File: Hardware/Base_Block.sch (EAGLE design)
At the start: 46 parts, among them Q1 BSS138, U2 FTS31XS-U, U4 TPS62065

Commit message: file cleanup
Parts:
- L1: value (none) -> 1.0uH
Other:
- moved on the sheet: C8
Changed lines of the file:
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@@
 <part name="C9" library="SparkFun-Capacitors" deviceset="4.7UF-6.3V-10%(0603)" device="0603" value="4.7uF"/>
 <part name="GND10" library="SparkFun-Aesthetics" deviceset="GND" device=""/>
-<part name="L1" library="SparkFun-Passives" deviceset="INDUCTOR" device=""/>
+<part name="L1" library="SparkFun-Passives" deviceset="INDUCTOR" device="" value="1.0uH"/>
 <part name="FID1" library="SparkFun-Aesthetics" deviceset="FIDUCIAL" device="1X2"/>
 <part name="FID2" library="SparkFun-Aesthetics" deviceset="FIDUCIAL" device="1X2"/>
@@
 <instance part="D4" gate="G$1" x="27.94" y="78.74" rot="R90"/>
 <instance part="SUPPLY3" gate="G$1" x="27.94" y="86.36"/>
-<instance part="C8" gate="G$1" x="38.1" y="66.04"/>
-<instance part="GND17" gate="1" x="38.1" y="50.8"/>
+<instance part="C8" gate="G$1" x="40.64" y="66.04"/>
+<instance part="GND17" gate="1" x="40.64" y="50.8"/>
 <instance part="U$1" gate="G$1" x="81.28" y="68.58" rot="MR0"/>
 <instance part="GND18" gate="1" x="60.96" y="50.8"/>
@@
 <pinref part="C8" gate="G$1" pin="2"/>
 <pinref part="GND17" gate="1" pin="GND"/>
-<wire x1="38.1" y1="53.34" x2="38.1" y2="63.5" width="0.1524" layer="91"/>
+<wire x1="40.64" y1="53.34" x2="40.64" y2="63.5" width="0.1524" layer="91"/>
 </segment>
 <segment>
@@
 <pinref part="L1" gate="G$1" pin="2"/>
 <wire x1="200.66" y1="83.82" x2="200.66" y2="86.36" width="0.1524" layer="91"/>
+<junction x="218.44" y="86.36"/>
 </segment>
 <segment>
@@
 <wire x1="27.94" y1="73.66" x2="27.94" y2="76.2" width="0.1524" layer="91"/>
 <pinref part="D4" gate="G$1" pin="A"/>
-<wire x1="27.94" y1="73.66" x2="38.1" y2="73.66" width="0.1524" layer="91"/>
+<wire x1="27.94" y1="73.66" x2="40.64" y2="73.66" width="0.1524" layer="91"/>
 <junction x="27.94" y="73.66"/>
 <pinref part="C8" gate="G$1" pin="1"/>
-<wire x1="38.1" y1="71.12" x2="38.1" y2="73.66" width="0.1524" layer="91"/>
+<wire x1="40.64" y1="71.12" x2="40.64" y2="73.66" width="0.1524" layer="91"/>
 <pinref part="U$1" gate="G$1" pin="VOUT"/>
-<wire x1="38.1" y1="73.66" x2="63.5" y2="73.66" width="0.1524" layer="91"/>
-<junction x="38.1" y="73.66"/>
+<wire x1="40.64" y1="73.66" x2="63.5" y2="73.66" width="0.1524" layer="91"/>
+<junction x="40.64" y="73.66"/>
 <label x="45.72" y="73.66" size="1.778" layer="95"/>
 </segment>

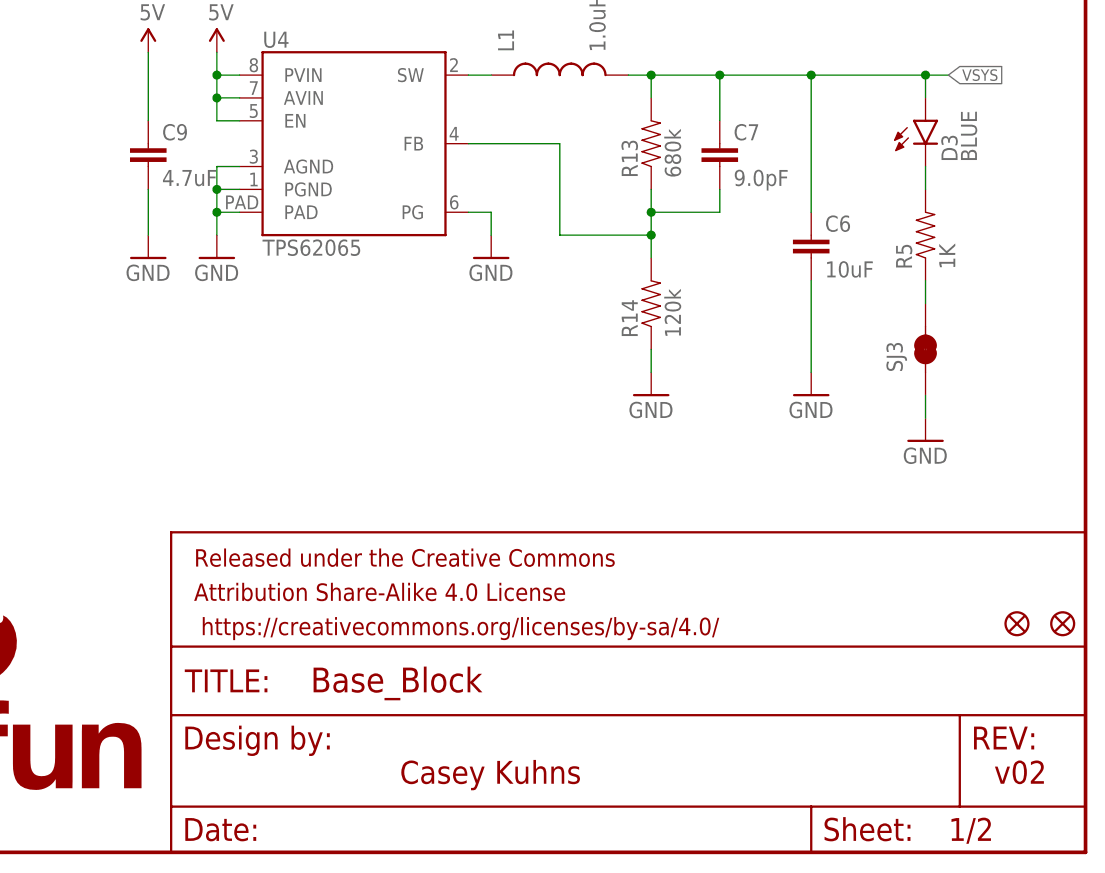
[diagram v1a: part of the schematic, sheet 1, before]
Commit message: Modified Footprint for connectors, removed jumpers. changed version number corrected silk moved diode to help AOI removed jumpers from power supply replaced input and output capacitors on power supply. replaced filtercap with 47pf
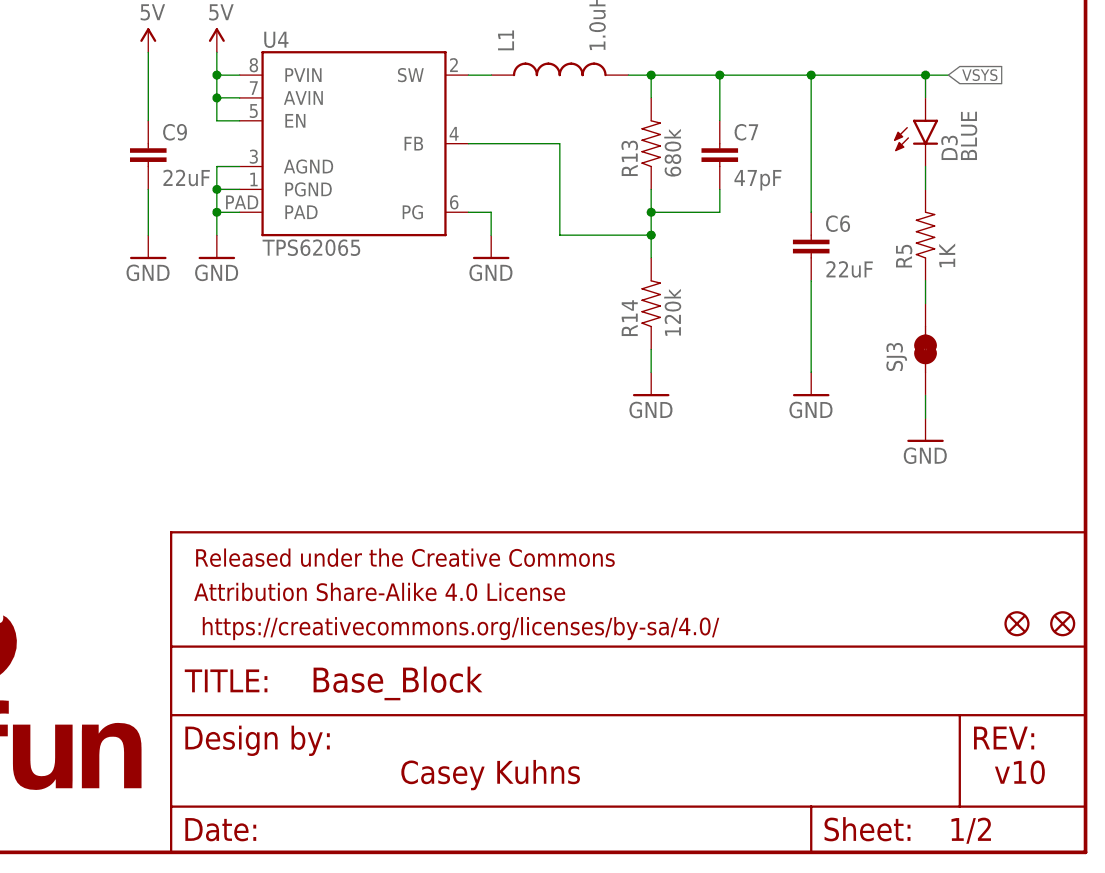
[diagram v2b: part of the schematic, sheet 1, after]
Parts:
- C6: value 10uF -> 22uF; device SparkFun-Capacitors:10UF-6.3V-20%(1206) -> SparkFun-Capacitors:22UF-6.3V-20%(0805)
- C7: value 9.0pF -> 47pF; device SparkFun-Capacitors:9.0PF-50V-10%(0603) -> SparkFun-Capacitors:47PF-50V-5%(0603)
- C9: value 4.7uF -> 22uF; device SparkFun-Capacitors:4.7UF-6.3V-10%(0603)0603 -> SparkFun-Capacitors:22UF-6.3V-20%(0805)
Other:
- note added: "v10"
- note removed: "v02"
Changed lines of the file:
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@@
 <?xml version="1.0" encoding="utf-8"?>
 <!DOCTYPE eagle SYSTEM "eagle.dtd">
-<eagle version="6.5.0">
+<eagle version="6.6.0">
 <drawing>
 <settings>
@@
 <part name="GND12" library="SparkFun-Aesthetics" deviceset="GND" device=""/>
 <part name="SJ3" library="SparkFun-Passives" deviceset="JUMPER-PAD-2-NC_BY_TRACE" device=""/>
-<part name="C6" library="SparkFun-Capacitors" deviceset="10UF-6.3V-20%(1206)" device="" value="10uF"/>
+<part name="C6" library="SparkFun-Capacitors" deviceset="22UF-6.3V-20%(0805)" device="" value="22uF"/>
 <part name="GND14" library="SparkFun-Aesthetics" deviceset="GND" device=""/>
 <part name="R6" library="SparkFun-Resistors" deviceset="100OHM1/10W1%(0603)" device="" value="100"/>
@@
 <part name="R13" library="SparkFun-Resistors" deviceset="RESISTOR" device="0603" value="680k"/>
 <part name="R14" library="SparkFun-Resistors" deviceset="RESISTOR" device="0603" value="120k"/>
-<part name="C7" library="SparkFun-Capacitors" deviceset="9.0PF-50V-10%(0603)" device="" value="9.0pF"/>
-<part name="C9" library="SparkFun-Capacitors" deviceset="4.7UF-6.3V-10%(0603)" device="0603" value="4.7uF"/>
+<part name="C7" library="SparkFun-Capacitors" deviceset="47PF-50V-5%(0603)" device="" value="47pF"/>
+<part name="C9" library="SparkFun-Capacitors" deviceset="22UF-6.3V-20%(0805)" device="" value="22uF"/>
 <part name="GND10" library="SparkFun-Aesthetics" deviceset="GND" device=""/>
 <part name="L1" library="SparkFun-Passives" deviceset="INDUCTOR" device="" value="1.0uH"/>
@@
 Prevents Battery board from enabling DCIN</text>
 <text x="172.72" y="7.62" size="2.54" layer="94">Casey Kuhns</text>
-<text x="238.76" y="7.62" size="2.54" layer="94">v02</text>
+<text x="238.76" y="7.62" size="2.54" layer="94">v10</text>
 </plain>
 <instances>
